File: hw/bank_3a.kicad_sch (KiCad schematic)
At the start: 2 parts, among them U1002 T20Q144xx

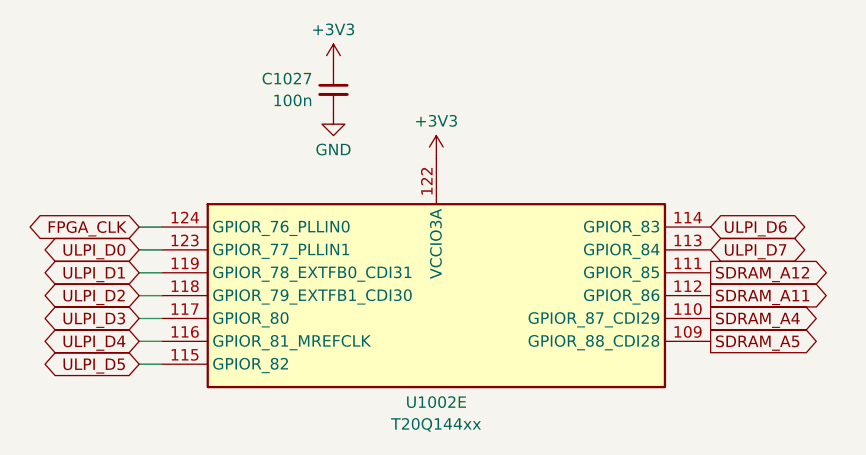
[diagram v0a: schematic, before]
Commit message: renumbered references on trion sub-sheets
Had used numbers > 1000 when merging designs
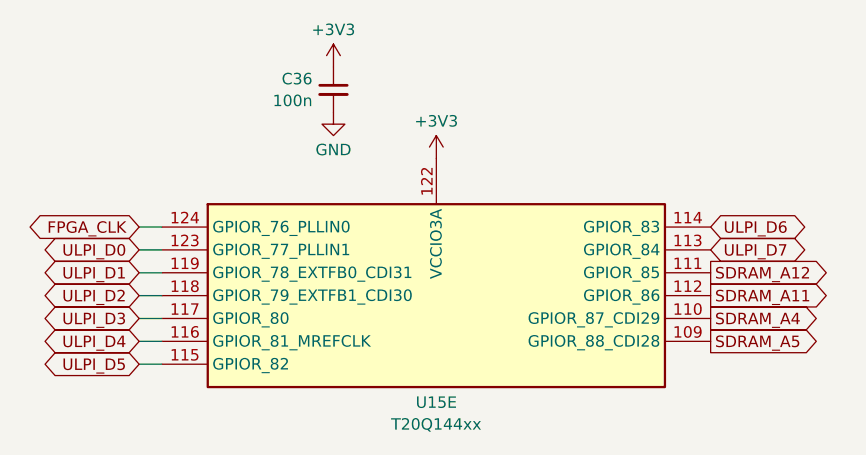
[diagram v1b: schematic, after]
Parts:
- renumbered C1027 to C36, U1002 to U15
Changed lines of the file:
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@@
   (symbol (lib_id "FPGA_Efinix_Trion:T8Q144xx") (at 146.05 95.885 0) (unit 5)
     (in_bom yes) (on_board yes) (dnp no) (fields_autoplaced)
-    (property "Reference" "U1002" (at 146.05 107.7651 0)
+    (property "Reference" "U15" (at 146.05 107.7651 0)
       (effects (font (size 1.27 1.27)))
     )
@@
       (project "usbadc"
         (path "/7c8a1f8d-8834-4c9b-aaae-1f231e9b09a1/d9cd2a48-41b0-4b01-a978-0843576735ad/945e4dbc-067e-402b-ba9d-38126a9e21c9"
-          (reference "U1002") (unit 5)
+          (reference "U15") (unit 5)
         )
       )
@@
   (symbol (lib_id "Device:C_Small") (at 134.62 73.025 0) (mirror y) (unit 1)
     (in_bom yes) (on_board yes) (dnp no) (fields_autoplaced)
-    (property "Reference" "C1027" (at 132.2959 71.8192 0)
+    (property "Reference" "C36" (at 132.2959 71.8192 0)
       (effects (font (size 1.27 1.27)) (justify left))
     )
@@
       (project "usbadc"
         (path "/7c8a1f8d-8834-4c9b-aaae-1f231e9b09a1/d9cd2a48-41b0-4b01-a978-0843576735ad/945e4dbc-067e-402b-ba9d-38126a9e21c9"
-          (reference "C1027") (unit 1)
-        )
-      )
+          (reference "C36") (unit 1)
+        )
+      )

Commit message: connected versaclock CLKSEL to ULPI RSTB (share FPGA pin)
ULPI Rstb is unlikely to be used

Also: - update of kicad to 9.0 (many library footprints updated)
      - added sheet titles, author
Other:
- company: (none) -> Till Straumann
- title: (none) -> FPGA Bank 3a
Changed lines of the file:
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@@
 (kicad_sch
-	(version 20231120)
+	(version 20250114)
 	(generator "eeschema")
-	(generator_version "8.0")
+	(generator_version "9.0")
 	(paper "A4")
+	(title_block
+		(title "FPGA Bank 3a")
+		(rev "3.3b")
+		(company "Till Straumann")
+	)
 	(wire
 		(pts

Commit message: Added licensing information
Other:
- company: Till Straumann -> Copyright Till Straumann, 2025
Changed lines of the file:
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@@
 		(title "FPGA Bank 3a")
 		(rev "3.3b")
-		(company "Till Straumann")
+		(company "Copyright Till Straumann, 2025")
+		(comment 1 "License: CERN-OHL-P v2")
 	)
 	(wire
